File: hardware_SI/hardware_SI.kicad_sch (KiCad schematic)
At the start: 39 parts

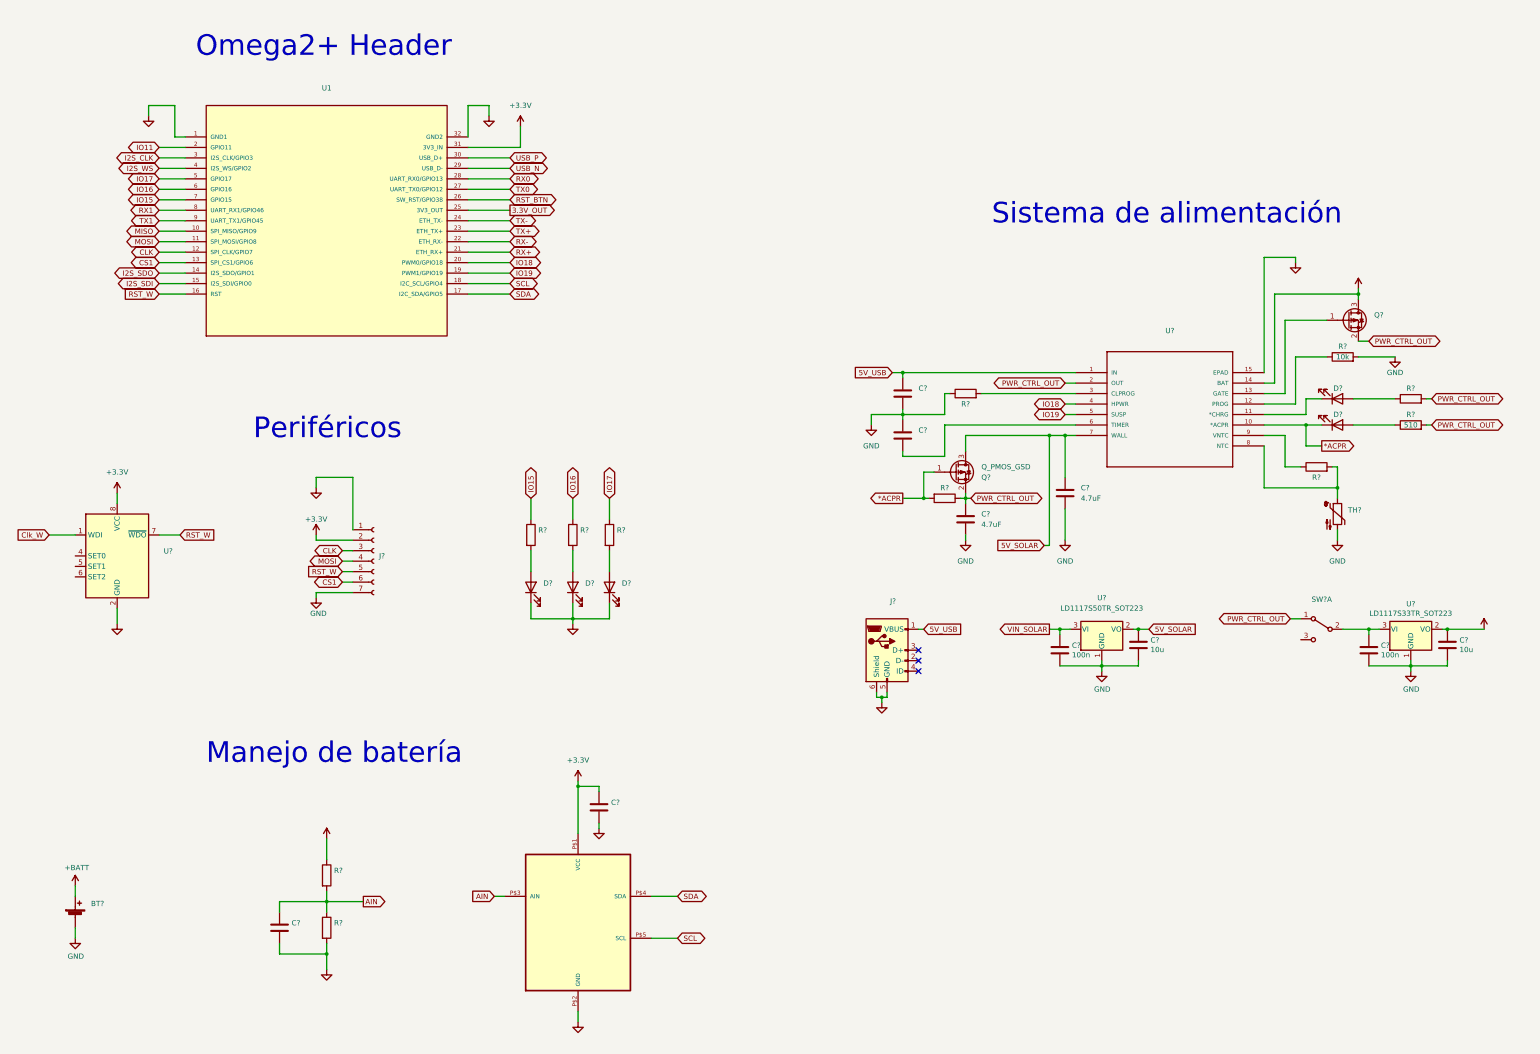
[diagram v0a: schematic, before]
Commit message: Conversor DC-DC y puerto panel solar
- Se agrega en el esquemático el puerto de entrada del panel solar y se conecta a un convertidor DC-DC
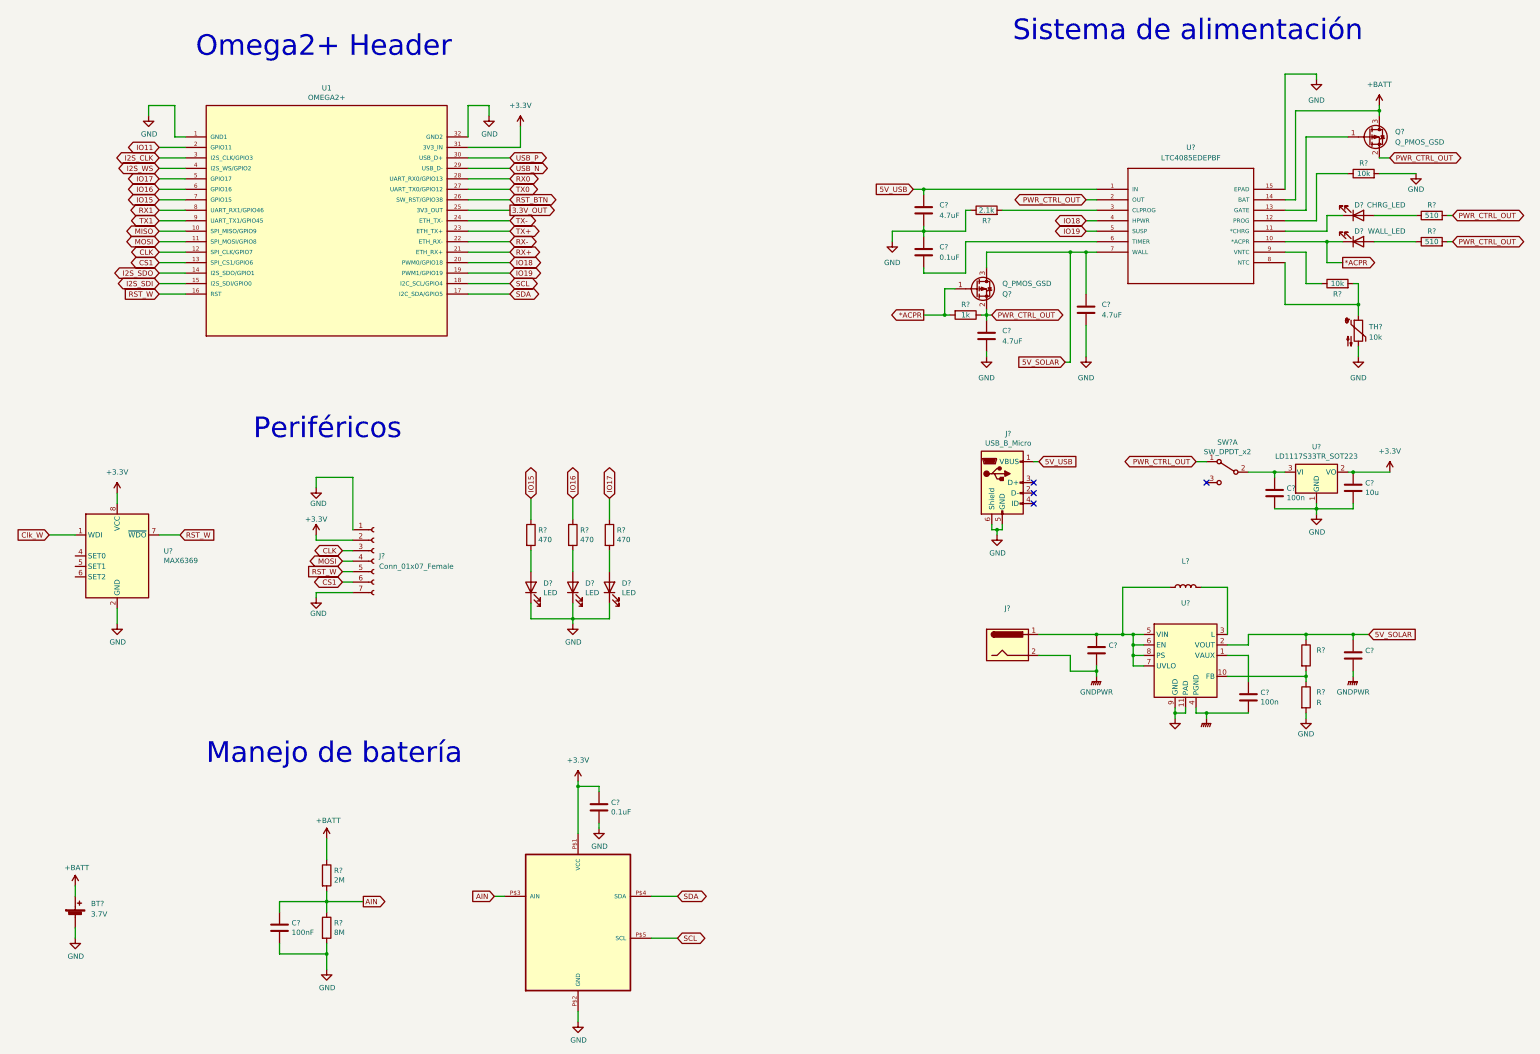
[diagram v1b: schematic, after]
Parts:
- removed C?: 10u, symbol Device:C
- removed C?: 100n, symbol Device:C
- removed U?: LD1117S50TR_SOT223, Package_TO_SOT_SMD:SOT-223-3_TabPin2, symbol Regulator_Linear:LD1117S50TR_SOT223
- added C? (x2): (no value), symbol Device:C
- added C?: 100n, symbol Device:C
- added J?: (no value), symbol Connector:Jack-DC
- added L?: (no value), symbol Device:L
- added R?: R, symbol Device:R
- added R?: (no value), symbol Device:R
- added U?: (no value), symbol Regulator_Switching:TPS61200DRC
- BT?: value (none) -> 3.7V
- C? (x2): value (none) -> 0.1uF
- C?: value (none) -> 100nF
- C?: value (none) -> 4.7uF
- D? (x3): value (none) -> LED
- D?: value (none) -> WALL_LED
- D?: value (none) -> CHRG_LED
- J?: value (none) -> USB_B_Micro
- J?: value (none) -> Conn_01x07_Female
- Q?: value (none) -> Q_PMOS_GSD
- R?: value (none) -> 2M
- R?: value (none) -> 8M
- R? (x3): value (none) -> 470
- R?: value (none) -> 510
- R?: value (none) -> 1k
- R?: value (none) -> 2.1k
- R?, TH?: value (none) -> 10k
- SW?: value (none) -> SW_DPDT_x2
- U1: value (none) -> OMEGA2+; footprint (none) -> Module:Onion_Omega2+
- U?: value (none) -> MCP3021; footprint (none) -> SOT-23
- U?: value (none) -> MAX6369; footprint (none) -> Package_TO_SOT_SMD:SOT-23-8
- U?: value (none) -> LTC4085EDEPBF; footprint (none) -> DFN-14_DE
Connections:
- net 5V_SOLAR: now also C?.1, R?.1, U?.2 (VOUT)
- net GND: now also R?.2, U?.11 (PAD), U?.9 (GND)
- new net: R?.1, R?.2, U?.10 (FB)
- new net: C?.1, U?.1 (VAUX)
- new net: L?.2, U?.3 (L)
- new net: C?.1, J?.1, L?.1, U?.5 (VIN), U?.6 (EN), U?.7 (UVLO), U?.8 (PS)
- new net GNDPWR: C?.2, C?.2, C?.2, J?.2, U?.4 (PGND)
- no-connect marks 3 -> 4
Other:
- moved on the sheet: C?, D?, J?, Q?, R?, SW?A, TH?, U?

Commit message: Asignación de huellas
- Se asignaron las huellas de los componentes del esquemático
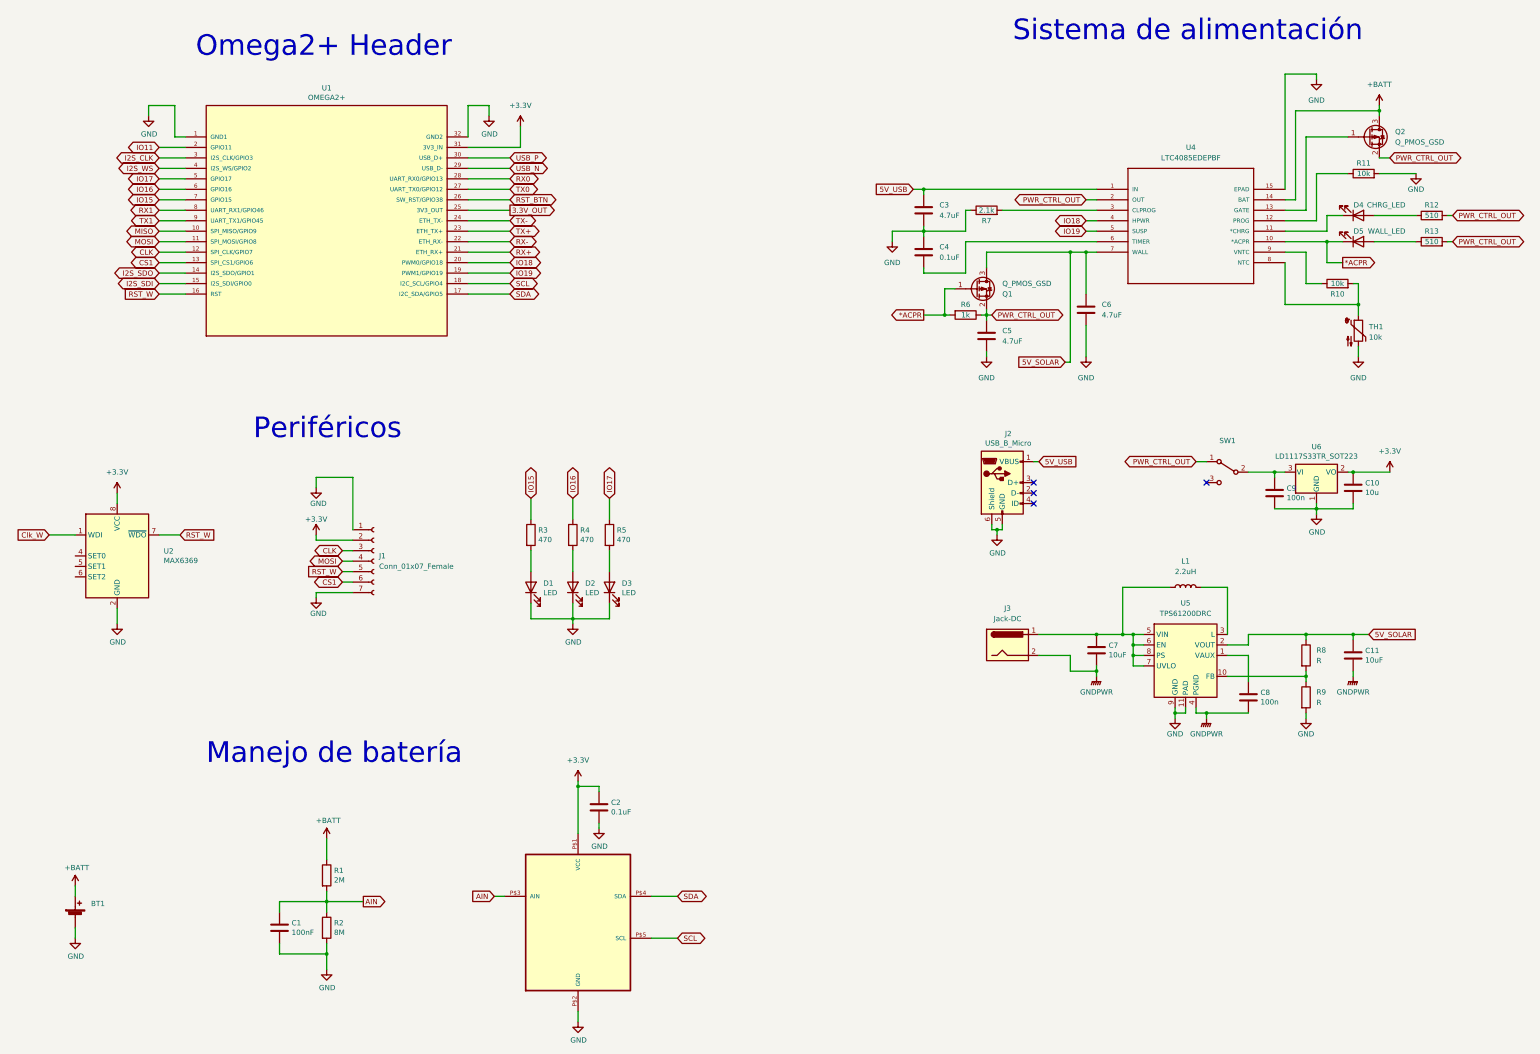
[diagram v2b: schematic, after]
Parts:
- removed SW?: SW_DPDT_x2, symbol Switch:SW_DPDT_x2
- added SW1: (no value), symbol Switch:SW_SPDT
- BT1: renamed from BT?; value 3.7V -> (none)
- C11, C7: renamed from C?; value (none) -> 10uF
- J3: renamed from J?; value (none) -> Jack-DC; footprint (none) -> Connector_BarrelJack:BarrelJack_SwitchcraftConxall_RAPC10U_Horizontal
- L1: renamed from L?; value (none) -> 2.2uH
- R8: renamed from R?; value (none) -> R
- U3: renamed from U?; footprint SOT-23 -> (none)
- U4: renamed from U?; footprint DFN-14_DE -> (none)
- U5: renamed from U?; value (none) -> TPS61200DRC; footprint (none) -> Package_SON:Texas_S-PVSON-N10_ThermalVias
- gave numbers to parts that had none: 33
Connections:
- net PWR_CTRL_OUT: now also SW1.1 (A)
- net at C9.1, U6.3 (VI): now also SW1.2 (B)

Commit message: Corrección de errores
- Se corrigen errores relacionados a conexiones y huellas.
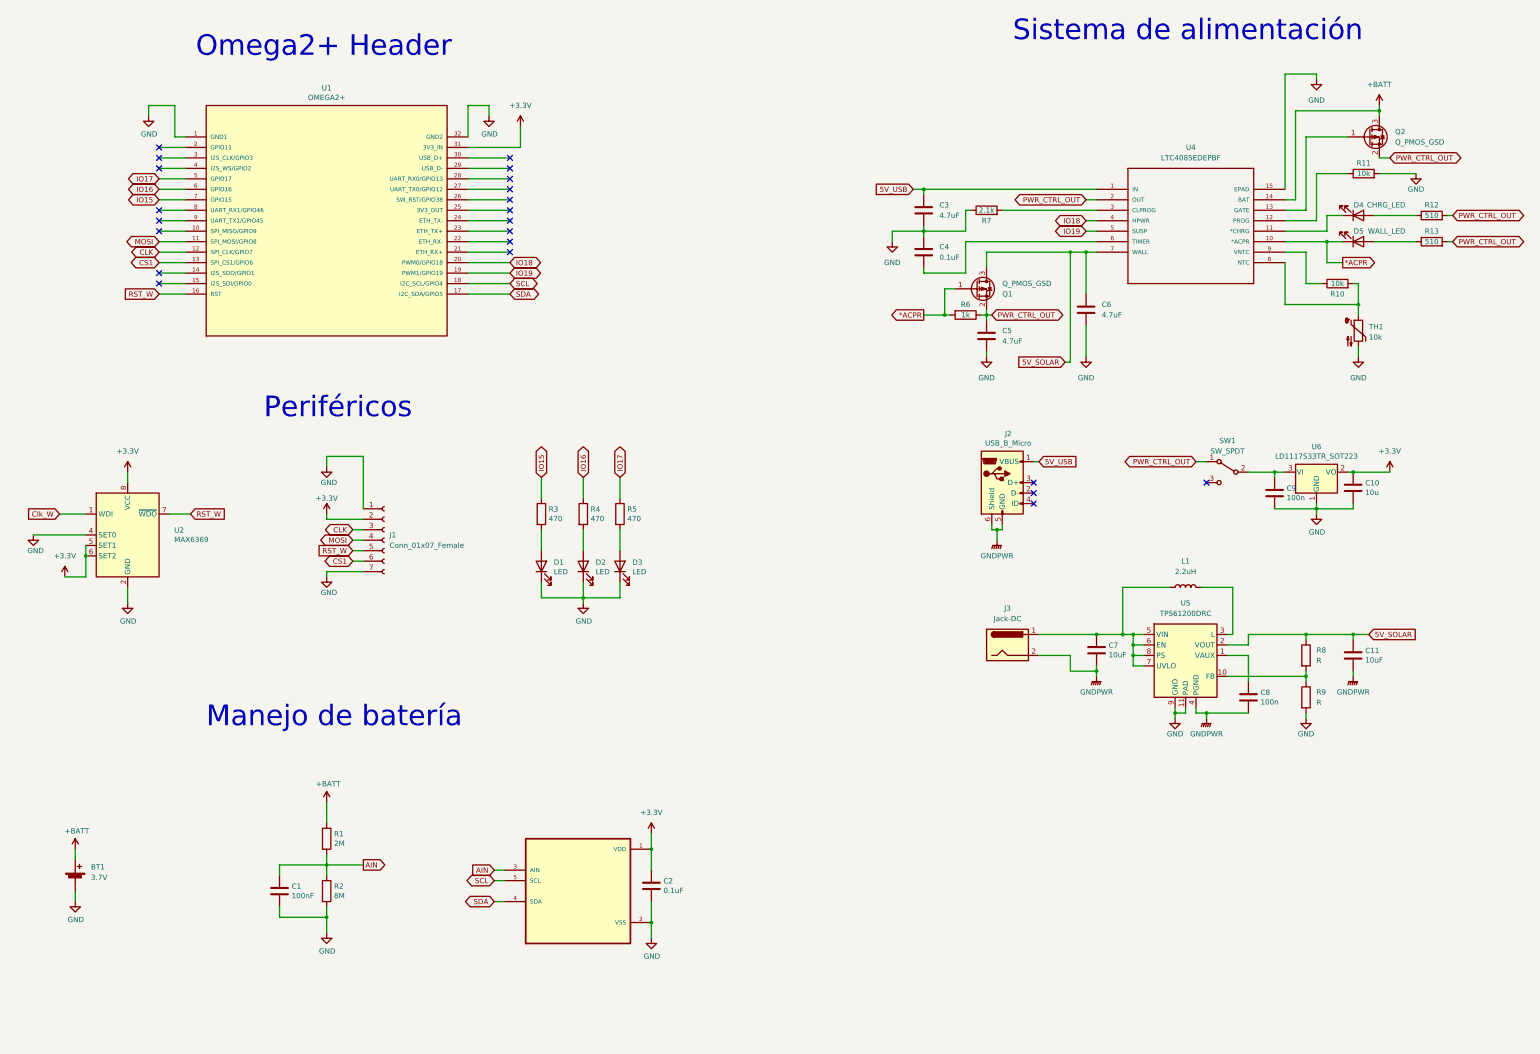
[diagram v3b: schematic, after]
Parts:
- BT1: value (none) -> 3.7V; footprint (none) -> Battery:BatteryHolder_MPD_BH-18650-PC2
- C1, C10, C11, C2, C3, C4, C5, C6, C7, C8, C9: footprint (none) -> Capacitor_SMD:C_0805_2012Metric_Pad1.18x1.45mm_HandSolder
- D1, D2, D3, D4, D5: footprint (none) -> LED_SMD:LED_0805_2012Metric_Pad1.15x1.40mm_HandSolder
- J1: footprint (none) -> Connector_PinSocket_2.54mm:PinSocket_1x07_P2.54mm_Vertical
- J2: footprint (none) -> Connector_USB:USB_Micro-B_Molex-105017-0001
- L1: footprint (none) -> Inductor_SMD:L_Coilcraft_LPS4018
- Q1, Q2: footprint (none) -> Package_TO_SOT_SMD:SOT-23_Handsoldering
- R1, R10, R11, R12, R13, R2, R3, R4, R5, R6, R7, R8, R9: footprint (none) -> Resistor_SMD:R_0805_2012Metric_Pad1.20x1.40mm_HandSolder
- SW1: value (none) -> SW_SPDT; footprint (none) -> Button_Switch_THT:SW_CuK_OS102011MA1QN1_SPDT_Angled
- TH1: footprint (none) -> Resistor_SMD:R_0603_1608Metric_Pad0.98x0.95mm_HandSolder
- U3: value MCP3021 -> (none); footprint (none) -> SOT95P270X145-5N; symbol hardware_SI-rescue:MCP3021-MCP3021 -> MCP3021A5T-E_OT:MCP3021A5T-E/OT
- U4: footprint (none) -> LTC4085EDEPBF:DFN-14_DE
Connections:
- net +3V3: now also U2.5 (SET1), U2.6 (SET2), U3.1 (VDD); no longer U3.P$1 (VCC)
- net AIN: now also U3.3 (AIN); no longer U3.P$3 (AIN)
- net GND: now also U2.4 (SET0), U3.2 (VSS); no longer J2.5 (GND), J2.6 (Shield), U3.P$2 (GND)
- net GNDPWR: now also J2.5 (GND), J2.6 (Shield)
- net SCL: now also U3.5 (SCL); no longer U3.P$5 (SCL)
- net SDA: now also U3.4 (SDA); no longer U3.P$4 (SDA)
- net 3.3V_OUT: no longer names the net of U1.25 (3V3_OUT)
- net I2S_CLK: no longer names the net of U1.3 (I2S_CLK/GPIO3)
- net I2S_SDI: no longer names the net of U1.15 (I2S_SDI/GPIO0)
- net I2S_SDO: no longer names the net of U1.14 (I2S_SDO/GPIO1)
- net I2S_WS: no longer names the net of U1.4 (I2S_WS/GPIO2)
- net IO11: no longer names the net of U1.2 (GPIO11)
- net MISO: no longer names the net of U1.10 (SPI_MISO/GPIO9)
- net RST_BTN: no longer names the net of U1.26 (SW_RST/GPIO38)
- net RX+: no longer names the net of U1.21 (ETH_RX+)
- net RX-: no longer names the net of U1.22 (ETH_RX-)
- net RX0: no longer names the net of U1.28 (UART_RX0/GPIO13)
- net RX1: no longer names the net of U1.8 (UART_RX1/GPIO46)
- net TX+: no longer names the net of U1.23 (ETH_TX+)
- net TX-: no longer names the net of U1.24 (ETH_TX-)
- net TX0: no longer names the net of U1.27 (UART_TX0/GPIO12)
- net TX1: no longer names the net of U1.9 (UART_TX1/GPIO45)
- net USB_N: no longer names the net of U1.29 (USB_D-)
- net USB_P: no longer names the net of U1.30 (USB_D+)
- no-connect marks 4 -> 22
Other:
- moved on the sheet: BT1, C1, C2, D1, D2, D3, J1, R1, R2, R3, R4, R5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
